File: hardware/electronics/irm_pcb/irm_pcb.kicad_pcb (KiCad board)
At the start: 2 copper layers, 128 x 81.3 mm, 63 parts, among them IC1 23LC1024, J1 Conn_01x04, J10 Conn_02x05_Counter_Clockwise, J11 Conn_01x04, J12 Conn_01x06, J13 Conn_01x06, J14 Conn_01x10, J16 Screw_Terminal_01x02, J17 Conn_01x06, J2 JUMPER_OPEN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

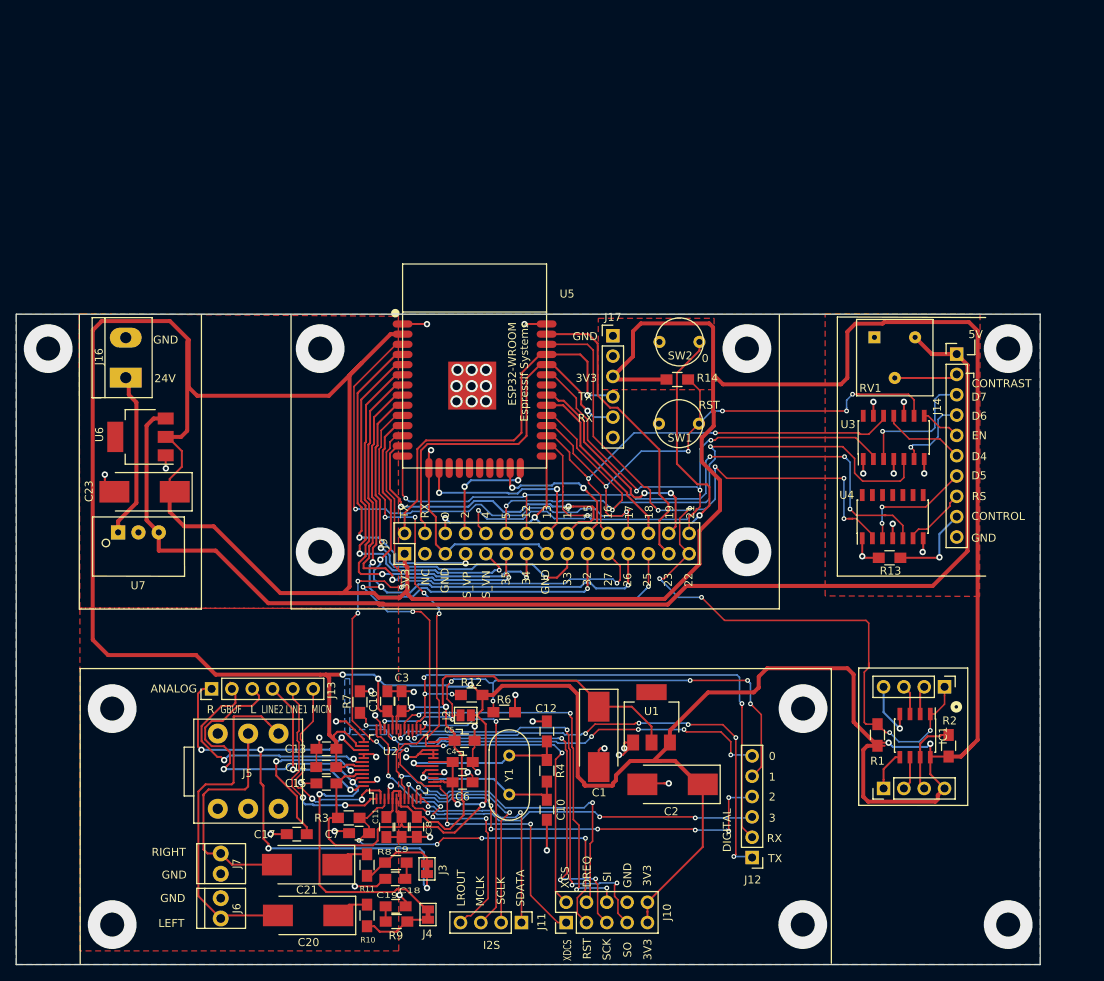
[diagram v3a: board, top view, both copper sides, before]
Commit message: Board size reduced
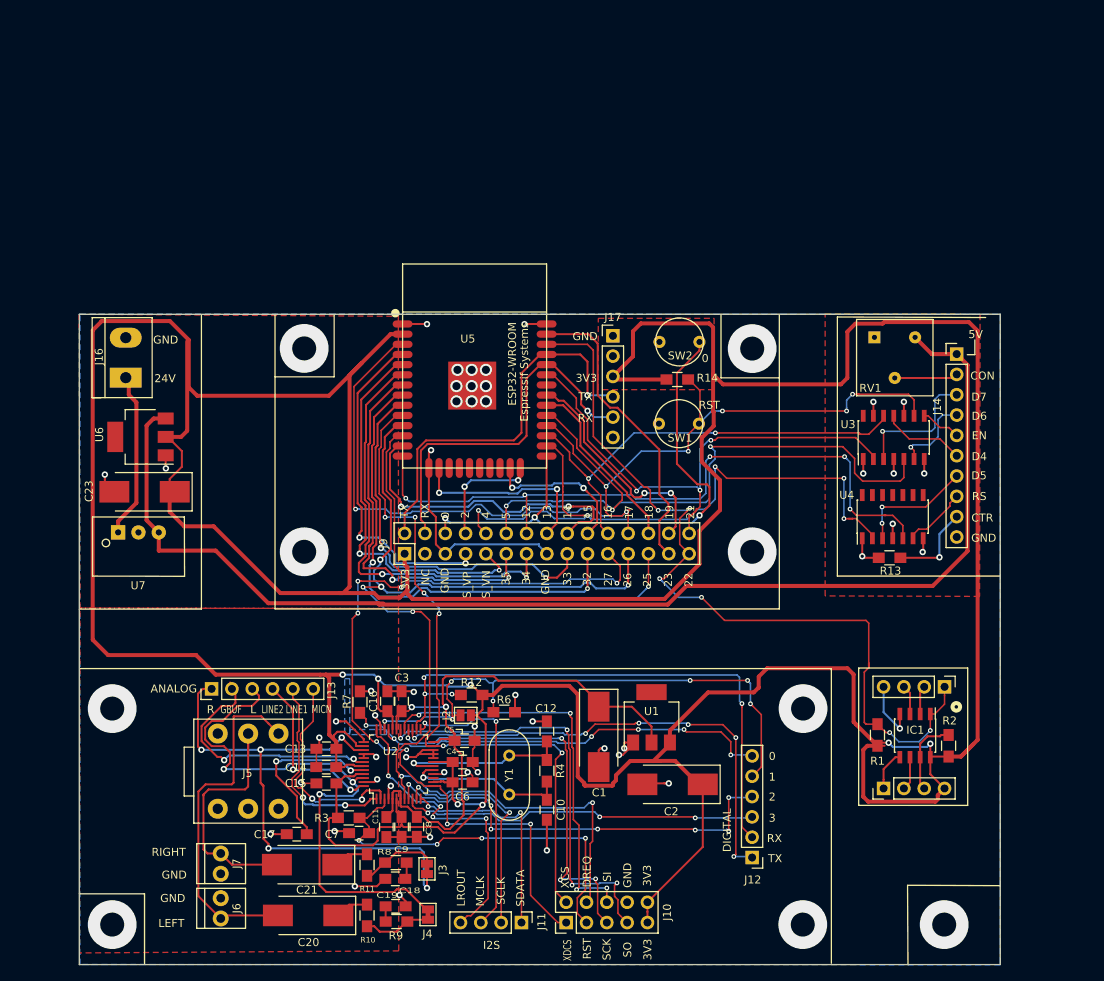
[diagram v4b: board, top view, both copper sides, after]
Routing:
- net (no net): vias 11 -> 9
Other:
- board size 128 x 81.3 mm -> 115.1 x 81.3 mm
- board text added: "CON"
- board text added: "CTR"
- board text removed: "CONTRAST"
- board text removed: "CONTROL"
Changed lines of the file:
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@@
   (general
     (thickness 1.6)
-    (drawings 115)
-    (tracks 1922)
+    (drawings 119)
+    (tracks 1920)
     (zones 0)
     (modules 63)
@@
     (tags "SOIC 1.27")
     (attr smd)
-    (fp_text reference IC1 (at 0 -3.5 90) (layer F.SilkS)
+    (fp_text reference IC1 (at -0.6985 -0.0254 180) (layer F.SilkS)
       (effects (font (size 1 1) (thickness 0.15)))
     )
@@
   (module irm_pcb:ESP32-WROOM-32-Espressif-Symbol-Kicad-62379 (layer F.Cu)
     (at 123.2995 53.176 180)
-    (fp_text reference U5 (at -11.557 9.017) (layer F.SilkS)
+    (fp_text reference U5 (at 0.8461 3.392) (layer F.SilkS)
       (effects (font (size 1 1) (thickness 0.15)))
     )
@@
     )
   )
+  (gr_line (start 177.419 118.0846) (end 177.4698 128.016) (layer F.SilkS) (width 0.12))
+  (gr_line (start 189.0014 118.1354) (end 177.419 118.0846) (layer F.SilkS) (width 0.12))
+  (gr_line (start 154.1018 54.6608) (end 154.1018 46.736) (layer F.SilkS) (width 0.12))
+  (gr_line (start 161.3662 54.6608) (end 154.1018 54.6608) (layer F.SilkS) (width 0.12))
+  (gr_line (start 82.042 119.1514) (end 82.042 127.9652) (layer F.SilkS) (width 0.12))
+  (gr_line (start 73.8886 119.1514) (end 82.042 119.1514) (layer F.SilkS) (width 0.12))
+  (gr_line (start 105.7402 54.5338) (end 105.7402 46.736) (layer F.SilkS) (width 0.12))
+  (gr_line (start 98.3488 54.5338) (end 105.7402 54.5338) (layer F.SilkS) (width 0.12))
   (gr_line (start 121.1072 101.3714) (end 121.8946 101.3714) (layer F.SilkS) (width 0.12))
   (gr_line (start 121.8946 101.3714) (end 121.8946 101.9048) (layer F.SilkS) (width 0.12))
@@
     (effects (font (size 1 1) (thickness 0.15)))
   )
-  (gr_text CONTROL (at 188.7474 71.9582) (layer F.SilkS)
+  (gr_text CTR (at 186.7662 72.1614) (layer F.SilkS)
     (effects (font (size 1 1) (thickness 0.15)))
   )
-  (gr_text RS (at 186.3598 69.469) (layer F.SilkS)
+  (gr_text RS (at 186.3852 69.469) (layer F.SilkS)
     (effects (font (size 1 1) (thickness 0.15)))
   )
@@
     (effects (font (size 1 1) (thickness 0.15)))
   )
-  (gr_line (start 185.6994 54.0766) (end 184.7342 54.102) (layer F.SilkS) (width 0.12))
-  (gr_line (start 185.6994 54.6354) (end 185.6994 54.0766) (layer F.SilkS) (width 0.12))
   (gr_line (start 185.8264 51.7652) (end 184.8866 51.7652) (layer F.SilkS) (width 0.12))
   (gr_line (start 185.8264 49.911) (end 185.8264 51.7652) (layer F.SilkS) (width 0.12))
-  (gr_text CONTRAST (at 189.1792 55.372) (layer F.SilkS)
+  (gr_text "CON\n" (at 186.7916 54.4068) (layer F.SilkS)
     (effects (font (size 1 1) (thickness 0.15)))
   )
@@
     (effects (font (size 1 1) (thickness 0.15)))
   )
-  (gr_line (start 74 91) (end 74 127.889) (layer F.SilkS) (width 0.12))
-  (gr_line (start 73.8886 46.7614) (end 73.8886 83.566) (layer F.SilkS) (width 0.12))
-  (gr_line (start 194 46.7) (end 194 128) (layer Edge.Cuts) (width 0.05))
-  (gr_line (start 66 128) (end 194 128) (layer Edge.Cuts) (width 0.05))
-  (gr_line (start 66 46.7) (end 194 46.7) (layer Edge.Cuts) (width 0.05))
-  (gr_line (start 66 46.7) (end 66 128) (layer Edge.Cuts) (width 0.05))
+  (gr_line (start 189 46.7) (end 189 128) (layer Edge.Cuts) (width 0.05))
+  (gr_line (start 73.8886 128) (end 189 128) (layer Edge.Cuts) (width 0.05))
+  (gr_line (start 73.8886 46.7106) (end 189 46.7) (layer Edge.Cuts) (width 0.05))
+  (gr_line (start 73.8886 46.7106) (end 73.8886 128) (layer Edge.Cuts) (width 0.05))
   (gr_line (start 119.888 52.5145) (end 120.015 52.5145) (layer B.Mask) (width 0.15))
   (gr_line (start 119.8245 58.8645) (end 119.888 52.5145) (layer B.Mask) (width 0.15))
@@
   (gr_line (start 184.9374 90.932) (end 171.3103 90.932) (layer F.SilkS) (width 0.12))
   (gr_line (start 187.1853 47.117) (end 168.6433 47.0535) (layer F.SilkS) (width 0.12))
-  (gr_line (start 168.6433 79.4385) (end 187.1853 79.4385) (layer F.SilkS) (width 0.12))
+  (gr_line (start 168.6433 79.4385) (end 189 79.4385) (layer F.SilkS) (width 0.12))
   (gr_line (start 168.6433 79.4385) (end 168.6433 47.0535) (layer F.SilkS) (width 0.1524))
-  (gr_line (start 100.3808 83.5406) (end 161.3916 83.5406) (layer F.SilkS) (width 0.1524))
-  (gr_line (start 100.3554 46.7106) (end 100.3554 83.5406) (layer F.SilkS) (width 0.1524))
+  (gr_line (start 98.3554 83.5406) (end 161.3916 83.5406) (layer F.SilkS) (width 0.1524))
+  (gr_line (start 98.3554 46.7106) (end 98.3554 83.5406) (layer F.SilkS) (width 0.1524))
   (gr_text RST (at 152.6286 58.0644) (layer F.SilkS)
     (effects (font (size 1 1) (thickness 0.15)))
@@
   (segment (start 109.442 100.1835) (end 109.442 99.8085) (width 0.25) (layer F.Cu) (net 1))
   (via (at 105.9815 97.5995) (size 0.8) (drill 0.4) (layers F.Cu B.Cu) (net 1))
-  (via (at 70 51) (size 6.1) (drill 3) (layers F.Cu B.Cu) (net 0))
-  (via (at 104 51) (size 6.1) (drill 3) (layers F.Cu B.Cu) (net 0))
-  (via (at 157.34 51) (size 6.1) (drill 3) (layers F.Cu B.Cu) (net 0))
-  (via (at 190 51) (size 6.1) (drill 3) (layers F.Cu B.Cu) (net 0))
-  (via (at 104 76.4) (size 6.1) (drill 3) (layers F.Cu B.Cu) (net 0))
-  (via (at 157.34 76.4) (size 6.1) (drill 3) (layers F.Cu B.Cu) (net 0))
+  (via (at 102 50.9778) (size 6.1) (drill 3) (layers F.Cu B.Cu) (net 0))
+  (via (at 158 51) (size 6.1) (drill 3) (layers F.Cu B.Cu) (net 0))
+  (via (at 102 76.4) (size 6.1) (drill 3) (layers F.Cu B.Cu) (net 0))
+  (via (at 158 76.4) (size 6.1) (drill 3) (layers F.Cu B.Cu) (net 0))
   (via (at 78 96) (size 6.1) (drill 3) (layers F.Cu B.Cu) (net 0))
   (via (at 78 123) (size 6.1) (drill 3) (layers F.Cu B.Cu) (net 0))
   (via (at 164.36 96) (size 6.1) (drill 3) (layers F.Cu B.Cu) (net 0))
   (via (at 164.32 123) (size 6.1) (drill 3) (layers F.Cu B.Cu) (net 0))
-  (via (at 190 123) (size 6.1) (drill 3) (layers F.Cu B.Cu) (net 0))
+  (via (at 182 123) (size 6.1) (drill 3) (layers F.Cu B.Cu) (net 0))
   (segment (start 113.542 96.9605) (end 113.542 98.5835) (width 0.25) (layer F.Cu) (net 2))
   (segment (start 114.173 96.3295) (end 113.542 96.9605) (width 0.25) (layer F.Cu) (net 2))
@@
     (polygon
       (pts
-        (xy 194.0052 46.7106) (xy 194.0052 127.9906) (xy 65.9892 127.9906) (xy 65.9892 46.7106)
+        (xy 189.0014 46.7106) (xy 189.0014 128.016) (xy 73.9648 127.9906) (xy 73.9648 46.7106)
       )
     )
@@
     (polygon
       (pts
-        (xy 74.1172 46.6344) (xy 113.7666 46.9646) (xy 113.792 83.4898) (xy 73.9648 83.439) (xy 73.8632 46.6344)
-        (xy 74.1426 46.6344)
+        (xy 113.7666 46.9646) (xy 113.792 83.4898) (xy 73.9648 83.439) (xy 73.8632 46.7106)
       )
     )
@@
     (polygon
       (pts
-        (xy 73.9648 83.439) (xy 113.792 83.4898) (xy 113.8174 126.2888) (xy 73.9648 126.2888)
+        (xy 73.9648 83.439) (xy 113.792 83.4898) (xy 113.8174 126.2888) (xy 73.914 126.5428)
       )
     )
